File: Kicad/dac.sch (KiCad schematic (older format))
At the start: 13 parts

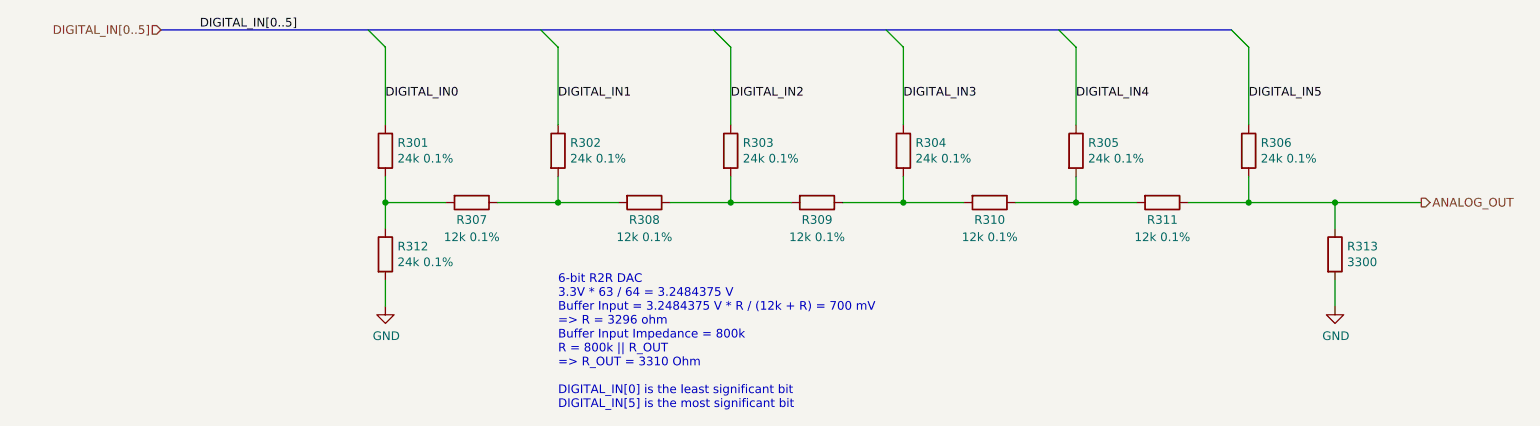
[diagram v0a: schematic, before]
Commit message: Added some part numbers.
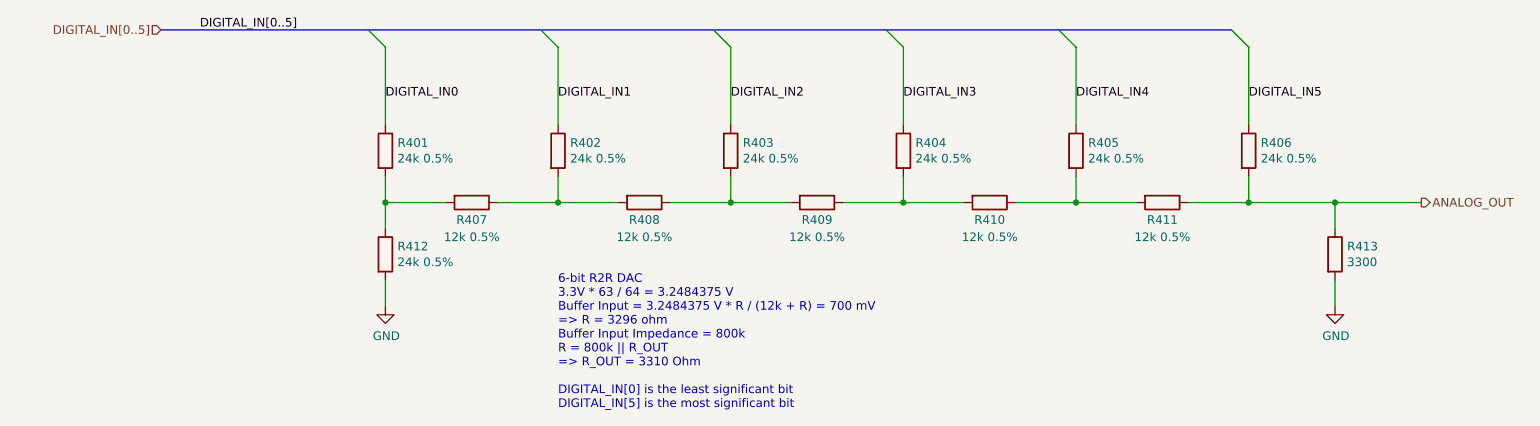
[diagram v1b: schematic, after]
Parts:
- R301, R302, R303, R304, R305, R306, R312: value 24k 0.1% -> 24k 0.5%; DNP (none) -> 0; Digikey (none) -> RNCF0805DTE24K0CT-ND; MPN (none) -> RNCF0805DTE24K0; Manufacturer (none) -> Stackpole
- R307, R308, R309, R310, R311: value 12k 0.1% -> 12k 0.5%; DNP (none) -> 0; Digikey (none) -> RNCF0805DTE12K0CT-ND; MPN (none) -> RNCF0805DTE12K0; Manufacturer (none) -> Stackpole
- R313: DNP (none) -> 0; Digikey (none) -> RMCF0805FG3K30-ND; MPN (none) -> RMCF0805FG3K30; Manufacturer (none) -> Stackpole
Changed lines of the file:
@@
 $Descr A4 11693 8268
 encoding utf-8
-Sheet 3 12
+Sheet 4 12
 Title "Neotron Common Hardware - VGA DAC"
 Date "2021-01-01"
@@
 AR Path="/5FDE658D/6009CBAC/5F5F4D05" Ref="R401"  Part="1"
 AR Path="/5FDE658D/600A04B7/5F5F4D05" Ref="R501"  Part="1"
-F 0 "R301" H 3570 2746 50  0000 L CNN
-F 1 "24k 0.1%" H 3570 2655 50  0000 L CNN
+F 0 "R401" H 3570 2746 50  0000 L CNN
+F 1 "24k 0.5%" H 3570 2655 50  0000 L CNN
 F 2 "Resistor_SMD:R_0805_2012Metric_Pad1.15x1.40mm_HandSolder" V 3430 2700 50  0001 C CNN
 F 3 "~" H 3500 2700 50  0001 C CNN
+F 4 "0" H 3500 2700 50  0001 C CNN "DNP"
+F 5 "RNCF0805DTE24K0CT-ND" H 3500 2700 50  0001 C CNN "Digikey"
+F 6 "RNCF0805DTE24K0" H 3500 2700 50  0001 C CNN "MPN"
+F 7 "Stackpole" H 3500 2700 50  0001 C CNN "Manufacturer"
 	1    3500 2700
 	1    0    0    -1
@@
 AR Path="/5FDE658D/6009CBAC/5F5F5C61" Ref="R407"  Part="1"
 AR Path="/5FDE658D/600A04B7/5F5F5C61" Ref="R507"  Part="1"
-F 0 "R307" V 4100 3000 50  0000 C CNN
-F 1 "12k 0.1%" V 4200 3000 50  0000 C CNN
+F 0 "R407" V 4100 3000 50  0000 C CNN
+F 1 "12k 0.5%" V 4200 3000 50  0000 C CNN
 F 2 "Resistor_SMD:R_0805_2012Metric_Pad1.15x1.40mm_HandSolder" V 3930 3000 50  0001 C CNN
 F 3 "~" H 4000 3000 50  0001 C CNN
+F 4 "0" H 4000 3000 50  0001 C CNN "DNP"
+F 5 "RNCF0805DTE12K0CT-ND" H 4000 3000 50  0001 C CNN "Digikey"
+F 6 "RNCF0805DTE12K0" H 4000 3000 50  0001 C CNN "MPN"
+F 7 "Stackpole" H 4000 3000 50  0001 C CNN "Manufacturer"
 	1    4000 3000
 	0    1    1    0
@@
 AR Path="/5FDE658D/6009CBAC/5F5F6568" Ref="R402"  Part="1"
 AR Path="/5FDE658D/600A04B7/5F5F6568" Ref="R502"  Part="1"
-F 0 "R302" H 4570 2746 50  0000 L CNN
-F 1 "24k 0.1%" H 4570 2655 50  0000 L CNN
+F 0 "R402" H 4570 2746 50  0000 L CNN
+F 1 "24k 0.5%" H 4570 2655 50  0000 L CNN
 F 2 "Resistor_SMD:R_0805_2012Metric_Pad1.15x1.40mm_HandSolder" V 4430 2700 50  0001 C CNN
 F 3 "~" H 4500 2700 50  0001 C CNN
+F 4 "0" H 4500 2700 50  0001 C CNN "DNP"
+F 5 "RNCF0805DTE24K0CT-ND" H 4500 2700 50  0001 C CNN "Digikey"
+F 6 "RNCF0805DTE24K0" H 4500 2700 50  0001 C CNN "MPN"
+F 7 "Stackpole" H 4500 2700 50  0001 C CNN "Manufacturer"
 	1    4500 2700
 	1    0    0    -1
@@
 AR Path="/5FDE658D/6009CBAC/5F5F6D42" Ref="R408"  Part="1"
 AR Path="/5FDE658D/600A04B7/5F5F6D42" Ref="R508"  Part="1"
-F 0 "R308" V 5100 3000 50  0000 C CNN
-F 1 "12k 0.1%" V 5200 3000 50  0000 C CNN
+F 0 "R408" V 5100 3000 50  0000 C CNN
+F 1 "12k 0.5%" V 5200 3000 50  0000 C CNN
 F 2 "Resistor_SMD:R_0805_2012Metric_Pad1.15x1.40mm_HandSolder" V 4930 3000 50  0001 C CNN
 F 3 "~" H 5000 3000 50  0001 C CNN
+F 4 "0" H 5000 3000 50  0001 C CNN "DNP"
+F 5 "RNCF0805DTE12K0CT-ND" H 5000 3000 50  0001 C CNN "Digikey"
+F 6 "RNCF0805DTE12K0" H 5000 3000 50  0001 C CNN "MPN"
+F 7 "Stackpole" H 5000 3000 50  0001 C CNN "Manufacturer"
 	1    5000 3000
 	0    1    1    0
@@
 AR Path="/5FDE658D/6009CBAC/5F5F6F45" Ref="R409"  Part="1"
 AR Path="/5FDE658D/600A04B7/5F5F6F45" Ref="R509"  Part="1"
-F 0 "R309" V 6100 3000 50  0000 C CNN
-F 1 "12k 0.1%" V 6200 3000 50  0000 C CNN
+F 0 "R409" V 6100 3000 50  0000 C CNN
+F 1 "12k 0.5%" V 6200 3000 50  0000 C CNN
 F 2 "Resistor_SMD:R_0805_2012Metric_Pad1.15x1.40mm_HandSolder" V 5930 3000 50  0001 C CNN
 F 3 "~" H 6000 3000 50  0001 C CNN
+F 4 "0" H 6000 3000 50  0001 C CNN "DNP"
+F 5 "RNCF0805DTE12K0CT-ND" H 6000 3000 50  0001 C CNN "Digikey"
+F 6 "RNCF0805DTE12K0" H 6000 3000 50  0001 C CNN "MPN"
+F 7 "Stackpole" H 6000 3000 50  0001 C CNN "Manufacturer"
 	1    6000 3000
 	0    1    1    0
@@
 AR Path="/5FDE658D/6009CBAC/5F5F984D" Ref="R410"  Part="1"
 AR Path="/5FDE658D/600A04B7/5F5F984D" Ref="R510"  Part="1"
-F 0 "R310" V 7100 3000 50  0000 C CNN
-F 1 "12k 0.1%" V 7200 3000 50  0000 C CNN
+F 0 "R410" V 7100 3000 50  0000 C CNN
+F 1 "12k 0.5%" V 7200 3000 50  0000 C CNN
 F 2 "Resistor_SMD:R_0805_2012Metric_Pad1.15x1.40mm_HandSolder" V 6930 3000 50  0001 C CNN
 F 3 "~" H 7000 3000 50  0001 C CNN
+F 4 "0" H 7000 3000 50  0001 C CNN "DNP"
+F 5 "RNCF0805DTE12K0CT-ND" H 7000 3000 50  0001 C CNN "Digikey"
+F 6 "RNCF0805DTE12K0" H 7000 3000 50  0001 C CNN "MPN"
+F 7 "Stackpole" H 7000 3000 50  0001 C CNN "Manufacturer"
 	1    7000 3000
 	0    1    1    0
@@
 AR Path="/5FDE658D/6009CBAC/5F5F99D6" Ref="R411"  Part="1"
 AR Path="/5FDE658D/600A04B7/5F5F99D6" Ref="R511"  Part="1"
-F 0 "R311" V 8100 3000 50  0000 C CNN
-F 1 "12k 0.1%" V 8200 3000 50  0000 C CNN
+F 0 "R411" V 8100 3000 50  0000 C CNN
+F 1 "12k 0.5%" V 8200 3000 50  0000 C CNN
 F 2 "Resistor_SMD:R_0805_2012Metric_Pad1.15x1.40mm_HandSolder" V 7930 3000 50  0001 C CNN
 F 3 "~" H 8000 3000 50  0001 C CNN
+F 4 "0" H 8000 3000 50  0001 C CNN "DNP"
+F 5 "RNCF0805DTE12K0CT-ND" H 8000 3000 50  0001 C CNN "Digikey"
+F 6 "RNCF0805DTE12K0" H 8000 3000 50  0001 C CNN "MPN"
+F 7 "Stackpole" H 8000 3000 50  0001 C CNN "Manufacturer"
 	1    8000 3000
 	0    1    1    0
@@
 AR Path="/5FDE658D/6009CBAC/5F5FA2EE" Ref="R413"  Part="1"
 AR Path="/5FDE658D/600A04B7/5F5FA2EE" Ref="R513"  Part="1"
-F 0 "R313" H 9070 3346 50  0000 L CNN
+F 0 "R413" H 9070 3346 50  0000 L CNN
 F 1 "3300" H 9070 3255 50  0000 L CNN
 F 2 "Resistor_SMD:R_0805_2012Metric_Pad1.15x1.40mm_HandSolder" V 8930 3300 50  0001 C CNN
 F 3 "~" H 9000 3300 50  0001 C CNN
+F 4 "0" H 9000 3300 50  0001 C CNN "DNP"
+F 5 "RMCF0805FG3K30-ND" H 9000 3300 50  0001 C CNN "Digikey"
+F 6 "RMCF0805FG3K30" H 9000 3300 50  0001 C CNN "MPN"
+F 7 "Stackpole" H 9000 3300 50  0001 C CNN "Manufacturer"
 	1    9000 3300
 	1    0    0    -1
@@
 AR Path="/5FDE658D/6009CBAC/5F5FBB89" Ref="#PWR0401"  Part="1"
 AR Path="/5FDE658D/600A04B7/5F5FBB89" Ref="#PWR0501"  Part="1"
-F 0 "#PWR0301" H 3500 3350 50  0001 C CNN
+F 0 "#PWR0401" H 3500 3350 50  0001 C CNN
 F 1 "GND" H 3505 3427 50  0000 C CNN
 F 2 "" H 3500 3600 50  0001 C CNN
@@
 AR Path="/5FDE658D/6009CBAC/5F5FBF42" Ref="#PWR0402"  Part="1"
 AR Path="/5FDE658D/600A04B7/5F5FBF42" Ref="#PWR0502"  Part="1"
-F 0 "#PWR0302" H 9000 3350 50  0001 C CNN
+F 0 "#PWR0402" H 9000 3350 50  0001 C CNN
 F 1 "GND" H 9005 3427 50  0000 C CNN
 F 2 "" H 9000 3600 50  0001 C CNN
@@
 AR Path="/5FDE658D/6009CBAC/5F5FCF8C" Ref="R412"  Part="1"
 AR Path="/5FDE658D/600A04B7/5F5FCF8C" Ref="R512"  Part="1"
-F 0 "R312" H 3570 3346 50  0000 L CNN
-F 1 "24k 0.1%" H 3570 3255 50  0000 L CNN
+F 0 "R412" H 3570 3346 50  0000 L CNN
+F 1 "24k 0.5%" H 3570 3255 50  0000 L CNN
 F 2 "Resistor_SMD:R_0805_2012Metric_Pad1.15x1.40mm_HandSolder" V 3430 3300 50  0001 C CNN
 F 3 "~" H 3500 3300 50  0001 C CNN
+F 4 "0" H 3500 3300 50  0001 C CNN "DNP"
+F 5 "RNCF0805DTE24K0CT-ND" H 3500 3300 50  0001 C CNN "Digikey"
+F 6 "RNCF0805DTE24K0" H 3500 3300 50  0001 C CNN "MPN"
+F 7 "Stackpole" H 3500 3300 50  0001 C CNN "Manufacturer"
 	1    3500 3300
 	1    0    0    -1
@@
 AR Path="/5FDE658D/6009CBAC/5F5FD13B" Ref="R403"  Part="1"
 AR Path="/5FDE658D/600A04B7/5F5FD13B" Ref="R503"  Part="1"
-F 0 "R303" H 5570 2746 50  0000 L CNN
-F 1 "24k 0.1%" H 5570 2655 50  0000 L CNN
+F 0 "R403" H 5570 2746 50  0000 L CNN
+F 1 "24k 0.5%" H 5570 2655 50  0000 L CNN
 F 2 "Resistor_SMD:R_0805_2012Metric_Pad1.15x1.40mm_HandSolder" V 5430 2700 50  0001 C CNN
 F 3 "~" H 5500 2700 50  0001 C CNN
+F 4 "0" H 5500 2700 50  0001 C CNN "DNP"
+F 5 "RNCF0805DTE24K0CT-ND" H 5500 2700 50  0001 C CNN "Digikey"
+F 6 "RNCF0805DTE24K0" H 5500 2700 50  0001 C CNN "MPN"
+F 7 "Stackpole" H 5500 2700 50  0001 C CNN "Manufacturer"
 	1    5500 2700
 	1    0    0    -1
@@
 AR Path="/5FDE658D/6009CBAC/5F5FD329" Ref="R404"  Part="1"
 AR Path="/5FDE658D/600A04B7/5F5FD329" Ref="R504"  Part="1"
-F 0 "R304" H 6570 2746 50  0000 L CNN
-F 1 "24k 0.1%" H 6570 2655 50  0000 L CNN
+F 0 "R404" H 6570 2746 50  0000 L CNN
+F 1 "24k 0.5%" H 6570 2655 50  0000 L CNN
 F 2 "Resistor_SMD:R_0805_2012Metric_Pad1.15x1.40mm_HandSolder" V 6430 2700 50  0001 C CNN
 F 3 "~" H 6500 2700 50  0001 C CNN
+F 4 "0" H 6500 2700 50  0001 C CNN "DNP"
+F 5 "RNCF0805DTE24K0CT-ND" H 6500 2700 50  0001 C CNN "Digikey"
+F 6 "RNCF0805DTE24K0" H 6500 2700 50  0001 C CNN "MPN"
+F 7 "Stackpole" H 6500 2700 50  0001 C CNN "Manufacturer"
 	1    6500 2700
 	1    0    0    -1
@@
 AR Path="/5FDE658D/6009CBAC/5F5FD46F" Ref="R405"  Part="1"
 AR Path="/5FDE658D/600A04B7/5F5FD46F" Ref="R505"  Part="1"
-F 0 "R305" H 7570 2746 50  0000 L CNN
-F 1 "24k 0.1%" H 7570 2655 50  0000 L CNN
+F 0 "R405" H 7570 2746 50  0000 L CNN
+F 1 "24k 0.5%" H 7570 2655 50  0000 L CNN
 F 2 "Resistor_SMD:R_0805_2012Metric_Pad1.15x1.40mm_HandSolder" V 7430 2700 50  0001 C CNN
 F 3 "~" H 7500 2700 50  0001 C CNN
+F 4 "0" H 7500 2700 50  0001 C CNN "DNP"
+F 5 "RNCF0805DTE24K0CT-ND" H 7500 2700 50  0001 C CNN "Digikey"
+F 6 "RNCF0805DTE24K0" H 7500 2700 50  0001 C CNN "MPN"
+F 7 "Stackpole" H 7500 2700 50  0001 C CNN "Manufacturer"
 	1    7500 2700
 	1    0    0    -1
@@
 AR Path="/5FDE658D/6009CBAC/5F5FD6C1" Ref="R406"  Part="1"
 AR Path="/5FDE658D/600A04B7/5F5FD6C1" Ref="R506"  Part="1"
-F 0 "R306" H 8570 2746 50  0000 L CNN
-F 1 "24k 0.1%" H 8570 2655 50  0000 L CNN
+F 0 "R406" H 8570 2746 50  0000 L CNN
+F 1 "24k 0.5%" H 8570 2655 50  0000 L CNN
 F 2 "Resistor_SMD:R_0805_2012Metric_Pad1.15x1.40mm_HandSolder" V 8430 2700 50  0001 C CNN
 F 3 "~" H 8500 2700 50  0001 C CNN
+F 4 "0" H 8500 2700 50  0001 C CNN "DNP"
+F 5 "RNCF0805DTE24K0CT-ND" H 8500 2700 50  0001 C CNN "Digikey"
+F 6 "RNCF0805DTE24K0" H 8500 2700 50  0001 C CNN "MPN"
+F 7 "Stackpole" H 8500 2700 50  0001 C CNN "Manufacturer"
 	1    8500 2700
 	1    0    0    -1

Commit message: Marked no-fit parts
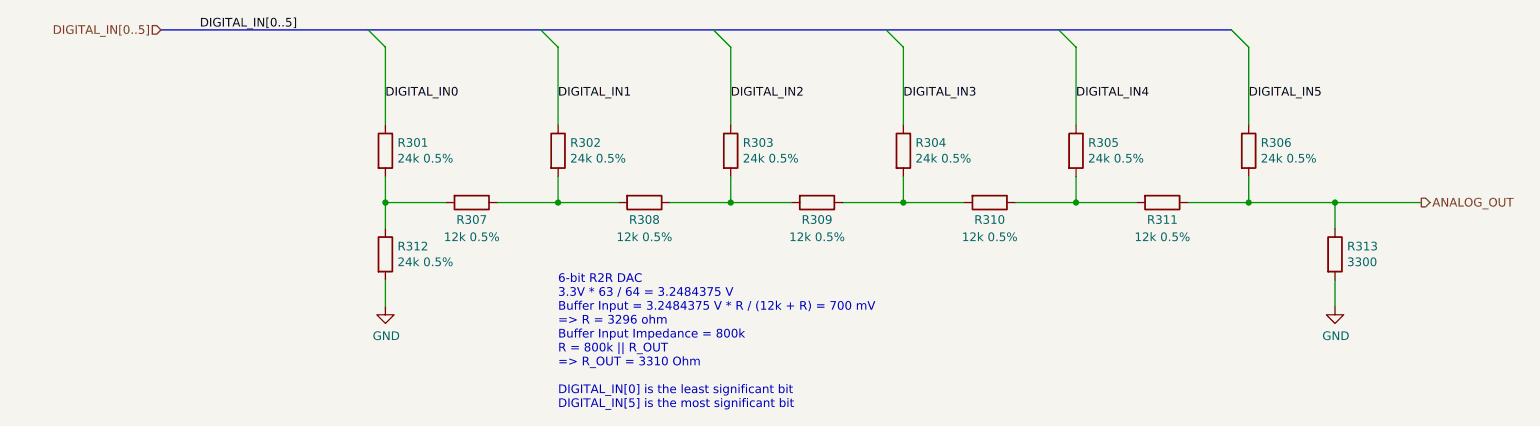
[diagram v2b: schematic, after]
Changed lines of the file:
@@
 $Descr A4 11693 8268
 encoding utf-8
-Sheet 4 12
+Sheet 3 12
 Title "Neotron Common Hardware - VGA DAC"
 Date "2021-01-01"
@@
 AR Path="/5FDE658D/6009CBAC/5F5F4D05" Ref="R401"  Part="1"
 AR Path="/5FDE658D/600A04B7/5F5F4D05" Ref="R501"  Part="1"
-F 0 "R401" H 3570 2746 50  0000 L CNN
+F 0 "R301" H 3570 2746 50  0000 L CNN
 F 1 "24k 0.5%" H 3570 2655 50  0000 L CNN
 F 2 "Resistor_SMD:R_0805_2012Metric_Pad1.15x1.40mm_HandSolder" V 3430 2700 50  0001 C CNN
@@
 AR Path="/5FDE658D/6009CBAC/5F5F5C61" Ref="R407"  Part="1"
 AR Path="/5FDE658D/600A04B7/5F5F5C61" Ref="R507"  Part="1"
-F 0 "R407" V 4100 3000 50  0000 C CNN
+F 0 "R307" V 4100 3000 50  0000 C CNN
 F 1 "12k 0.5%" V 4200 3000 50  0000 C CNN
 F 2 "Resistor_SMD:R_0805_2012Metric_Pad1.15x1.40mm_HandSolder" V 3930 3000 50  0001 C CNN
@@
 AR Path="/5FDE658D/6009CBAC/5F5F6568" Ref="R402"  Part="1"
 AR Path="/5FDE658D/600A04B7/5F5F6568" Ref="R502"  Part="1"
-F 0 "R402" H 4570 2746 50  0000 L CNN
+F 0 "R302" H 4570 2746 50  0000 L CNN
 F 1 "24k 0.5%" H 4570 2655 50  0000 L CNN
 F 2 "Resistor_SMD:R_0805_2012Metric_Pad1.15x1.40mm_HandSolder" V 4430 2700 50  0001 C CNN
@@
 AR Path="/5FDE658D/6009CBAC/5F5F6D42" Ref="R408"  Part="1"
 AR Path="/5FDE658D/600A04B7/5F5F6D42" Ref="R508"  Part="1"
-F 0 "R408" V 5100 3000 50  0000 C CNN
+F 0 "R308" V 5100 3000 50  0000 C CNN
 F 1 "12k 0.5%" V 5200 3000 50  0000 C CNN
 F 2 "Resistor_SMD:R_0805_2012Metric_Pad1.15x1.40mm_HandSolder" V 4930 3000 50  0001 C CNN
@@
 AR Path="/5FDE658D/6009CBAC/5F5F6F45" Ref="R409"  Part="1"
 AR Path="/5FDE658D/600A04B7/5F5F6F45" Ref="R509"  Part="1"
-F 0 "R409" V 6100 3000 50  0000 C CNN
+F 0 "R309" V 6100 3000 50  0000 C CNN
 F 1 "12k 0.5%" V 6200 3000 50  0000 C CNN
 F 2 "Resistor_SMD:R_0805_2012Metric_Pad1.15x1.40mm_HandSolder" V 5930 3000 50  0001 C CNN
@@
 AR Path="/5FDE658D/6009CBAC/5F5F984D" Ref="R410"  Part="1"
 AR Path="/5FDE658D/600A04B7/5F5F984D" Ref="R510"  Part="1"
-F 0 "R410" V 7100 3000 50  0000 C CNN
+F 0 "R310" V 7100 3000 50  0000 C CNN
 F 1 "12k 0.5%" V 7200 3000 50  0000 C CNN
 F 2 "Resistor_SMD:R_0805_2012Metric_Pad1.15x1.40mm_HandSolder" V 6930 3000 50  0001 C CNN
@@
 AR Path="/5FDE658D/6009CBAC/5F5F99D6" Ref="R411"  Part="1"
 AR Path="/5FDE658D/600A04B7/5F5F99D6" Ref="R511"  Part="1"
-F 0 "R411" V 8100 3000 50  0000 C CNN
+F 0 "R311" V 8100 3000 50  0000 C CNN
 F 1 "12k 0.5%" V 8200 3000 50  0000 C CNN
 F 2 "Resistor_SMD:R_0805_2012Metric_Pad1.15x1.40mm_HandSolder" V 7930 3000 50  0001 C CNN
@@
 AR Path="/5FDE658D/6009CBAC/5F5FA2EE" Ref="R413"  Part="1"
 AR Path="/5FDE658D/600A04B7/5F5FA2EE" Ref="R513"  Part="1"
-F 0 "R413" H 9070 3346 50  0000 L CNN
+F 0 "R313" H 9070 3346 50  0000 L CNN
 F 1 "3300" H 9070 3255 50  0000 L CNN
 F 2 "Resistor_SMD:R_0805_2012Metric_Pad1.15x1.40mm_HandSolder" V 8930 3300 50  0001 C CNN
@@
 AR Path="/5FDE658D/6009CBAC/5F5FBB89" Ref="#PWR0401"  Part="1"
 AR Path="/5FDE658D/600A04B7/5F5FBB89" Ref="#PWR0501"  Part="1"
-F 0 "#PWR0401" H 3500 3350 50  0001 C CNN
+F 0 "#PWR0301" H 3500 3350 50  0001 C CNN
 F 1 "GND" H 3505 3427 50  0000 C CNN
 F 2 "" H 3500 3600 50  0001 C CNN
@@
 AR Path="/5FDE658D/6009CBAC/5F5FBF42" Ref="#PWR0402"  Part="1"
 AR Path="/5FDE658D/600A04B7/5F5FBF42" Ref="#PWR0502"  Part="1"
-F 0 "#PWR0402" H 9000 3350 50  0001 C CNN
+F 0 "#PWR0302" H 9000 3350 50  0001 C CNN
 F 1 "GND" H 9005 3427 50  0000 C CNN
 F 2 "" H 9000 3600 50  0001 C CNN
@@
 AR Path="/5FDE658D/6009CBAC/5F5FCF8C" Ref="R412"  Part="1"
 AR Path="/5FDE658D/600A04B7/5F5FCF8C" Ref="R512"  Part="1"
-F 0 "R412" H 3570 3346 50  0000 L CNN
+F 0 "R312" H 3570 3346 50  0000 L CNN
 F 1 "24k 0.5%" H 3570 3255 50  0000 L CNN
 F 2 "Resistor_SMD:R_0805_2012Metric_Pad1.15x1.40mm_HandSolder" V 3430 3300 50  0001 C CNN
@@
 AR Path="/5FDE658D/6009CBAC/5F5FD13B" Ref="R403"  Part="1"
 AR Path="/5FDE658D/600A04B7/5F5FD13B" Ref="R503"  Part="1"
-F 0 "R403" H 5570 2746 50  0000 L CNN
+F 0 "R303" H 5570 2746 50  0000 L CNN
 F 1 "24k 0.5%" H 5570 2655 50  0000 L CNN
 F 2 "Resistor_SMD:R_0805_2012Metric_Pad1.15x1.40mm_HandSolder" V 5430 2700 50  0001 C CNN
@@
 AR Path="/5FDE658D/6009CBAC/5F5FD329" Ref="R404"  Part="1"
 AR Path="/5FDE658D/600A04B7/5F5FD329" Ref="R504"  Part="1"
-F 0 "R404" H 6570 2746 50  0000 L CNN
+F 0 "R304" H 6570 2746 50  0000 L CNN
 F 1 "24k 0.5%" H 6570 2655 50  0000 L CNN
 F 2 "Resistor_SMD:R_0805_2012Metric_Pad1.15x1.40mm_HandSolder" V 6430 2700 50  0001 C CNN
@@
 AR Path="/5FDE658D/6009CBAC/5F5FD46F" Ref="R405"  Part="1"
 AR Path="/5FDE658D/600A04B7/5F5FD46F" Ref="R505"  Part="1"
-F 0 "R405" H 7570 2746 50  0000 L CNN
+F 0 "R305" H 7570 2746 50  0000 L CNN
 F 1 "24k 0.5%" H 7570 2655 50  0000 L CNN
 F 2 "Resistor_SMD:R_0805_2012Metric_Pad1.15x1.40mm_HandSolder" V 7430 2700 50  0001 C CNN
@@
 AR Path="/5FDE658D/6009CBAC/5F5FD6C1" Ref="R406"  Part="1"
 AR Path="/5FDE658D/600A04B7/5F5FD6C1" Ref="R506"  Part="1"
-F 0 "R406" H 8570 2746 50  0000 L CNN
+F 0 "R306" H 8570 2746 50  0000 L CNN
 F 1 "24k 0.5%" H 8570 2655 50  0000 L CNN
 F 2 "Resistor_SMD:R_0805_2012Metric_Pad1.15x1.40mm_HandSolder" V 8430 2700 50  0001 C CNN
